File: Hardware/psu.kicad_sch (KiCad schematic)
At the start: 25 parts, among them U3 MP1584EN-LF-P, U4 AMS1117

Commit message: Reannotated
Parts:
- removed D4: D, symbol Device:D
- added D5: SMF3.3A, Diode_SMD:D_SMF, symbol Diode:SMF30A
- renumbered C5 to C10, C6 to C11, C8 to C12, C7 to C5, C9 to C6, C10 to C7, C16 to C8, C4 to C9, D5 to D13, D1 to D3, D3 to D4, D2 to D6, F2 to F1, F1 to F2, R7 to R12, R11 to R13, R8 to R14, R9 to R15, R10 to R16, R15 to R17, R16 to R35, U3 to U5
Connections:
- net +3V3: now also D5.1 (A1)
- net GND: now also D5.2 (A2)

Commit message: Pretty much all components now have values
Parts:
- C10, C9: value C_Polarized -> 100u
- C11, C5, C7, C8: value C -> 100n
- C12: value C -> 150p
- C6: value C_Polarized -> 220u
- D13: value LED -> RED
- D3: value D_Schottky -> SS54
- D4: value D -> B340A-13-F
- F1: value Fuse -> 32V?
- F2: value Fuse -> 1A
- L2: value L -> 15uH/3A
- R12: value R_Small -> 100k
- R13: value R -> 210k
- R14: value R_Small -> 24.9k
- R15, R16: value R -> 100k
- R17: value R -> 40.2k
- R35: value R -> 1k
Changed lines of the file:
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@@
 			)
 		)
-		(property "Value" "Fuse"
+		(property "Value" "32V?"
 			(at 182.88 52.1278 90)
 			(effects
@@
 			)
 		)
-		(property "Value" "R_Small"
+		(property "Value" "100k"
 			(at 113.2586 72.3321 0)
 			(effects
@@
 			)
 		)
-		(property "Value" "R"
+		(property "Value" "1k"
 			(at 231.648 59.6321 0)
 			(effects
@@
 			)
 		)
-		(property "Value" "L"
+		(property "Value" "15uH/3A"
 			(at 162.56 52.07 90)
 			(effects
@@
 			)
 		)
-		(property "Value" "C"
+		(property "Value" "100n"
 			(at 142.24 50.7308 90)
 			(effects
@@
 			)
 		)
-		(property "Value" "Fuse"
+		(property "Value" "1A"
 			(at 59.69 63.5578 90)
 			(effects
@@
 			)
 		)
-		(property "Value" "D_Schottky"
+		(property "Value" "SS54"
 			(at 70.1675 63.0498 0)
 			(effects
@@
 			)
 		)
-		(property "Value" "R_Small"
+		(property "Value" "24.9k"
 			(at 113.2586 83.7621 0)
 			(effects
@@
 			)
 		)
-		(property "Value" "R"
+		(property "Value" "40.2k"
 			(at 177.038 86.3021 0)
 			(effects
@@
 			)
 		)
-		(property "Value" "C"
+		(property "Value" "100n"
 			(at 105.791 77.4121 0)
 			(effects
@@
 			)
 		)
-		(property "Value" "R"
+		(property "Value" "100k"
 			(at 151.638 86.3021 0)
 			(effects
@@
 			)
 		)
-		(property "Value" "LED"
+		(property "Value" "RED"
 			(at 232.791 71.3796 90)
 			(effects
@@
 			)
 		)
-		(property "Value" "R"
+		(property "Value" "210k"
 			(at 177.8 67.31 90)
 			(effects
@@
 			)
 		)
-		(property "Value" "C"
+		(property "Value" "100n"
 			(at 223.901 64.7121 0)
 			(effects
@@
 			)
 		)
-		(property "Value" "C_Polarized"
+		(property "Value" "220u"
 			(at 171.831 61.2831 0)
 			(effects
@@
 			)
 		)
-		(property "Value" "C"
+		(property "Value" "100n"
 			(at 193.421 63.4421 0)
 			(effects
@@
 			)
 		)
-		(property "Value" "C_Polarized"
+		(property "Value" "100u"
 			(at 98.171 76.5231 0)
 			(effects
@@
 			)
 		)
-		(property "Value" "C"
+		(property "Value" "150p"
 			(at 152.781 76.1421 0)
 			(effects
@@
 			)
 		)
-		(property "Value" "D"
+		(property "Value" "B340A-13-F"
 			(at 158.242 62.1721 90)
 			(effects
@@
 			)
 		)
-		(property "Value" "R"
+		(property "Value" "100k"
 			(at 123.698 79.9521 0)
 			(effects
@@
 			)
 		)
-		(property "Value" "C_Polarized"
+		(property "Value" "100u"
 			(at 89.281 76.5231 0)
 			(effects

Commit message: Second cut of circuit board
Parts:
- C11, C12, C5, C7, C8: footprint (none) -> Capacitor_SMD:C_0603_1608Metric
- D13: footprint (none) -> LED_SMD:LED_0603_1608Metric
- D3, D4: footprint (none) -> Diode_SMD:D_SMA
- L2: footprint (none) -> Inductor_SMD:L_SXN_SMDRI64
- R12, R13, R14, R15, R16, R17, R35: footprint (none) -> Resistor_SMD:R_0603_1608Metric
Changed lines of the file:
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@@
 			)
 		)
-		(property "Footprint" ""
+		(property "Footprint" "Resistor_SMD:R_0603_1608Metric"
 			(at 111.76 71.12 0)
 			(effects
@@
 			)
 		)
-		(property "Footprint" ""
+		(property "Footprint" "Resistor_SMD:R_0603_1608Metric"
 			(at 228.092 58.42 90)
 			(effects
@@
 			)
 		)
-		(property "Footprint" ""
+		(property "Footprint" "Inductor_SMD:L_SXN_SMDRI64"
 			(at 162.56 54.61 0)
 			(effects
@@
 			)
 		)
-		(property "Footprint" ""
+		(property "Footprint" "Capacitor_SMD:C_0603_1608Metric"
 			(at 146.05 53.6448 0)
 			(effects
@@
 			)
 		)
-		(property "Footprint" ""
+		(property "Footprint" "Diode_SMD:D_SMA"
 			(at 69.85 66.04 0)
 			(effects
@@
 			)
 		)
-		(property "Footprint" ""
+		(property "Footprint" "Resistor_SMD:R_0603_1608Metric"
 			(at 111.76 82.55 0)
 			(effects
@@
 			)
 		)
-		(property "Footprint" ""
+		(property "Footprint" "Resistor_SMD:R_0603_1608Metric"
 			(at 173.482 85.09 90)
 			(effects
@@
 			)
 		)
-		(property "Footprint" ""
+		(property "Footprint" "Capacitor_SMD:C_0603_1608Metric"
 			(at 101.9048 72.39 0)
 			(effects
@@
 			)
 		)
-		(property "Footprint" ""
+		(property "Footprint" "Resistor_SMD:R_0603_1608Metric"
 			(at 148.082 85.09 90)
 			(effects
@@
 			)
 		)
-		(property "Footprint" ""
+		(property "Footprint" "LED_SMD:LED_0603_1608Metric"
 			(at 229.87 68.58 0)
 			(effects
@@
 			)
 		)
-		(property "Footprint" ""
+		(property "Footprint" "Resistor_SMD:R_0603_1608Metric"
 			(at 173.482 67.31 90)
 			(effects
@@
 			)
 		)
-		(property "Footprint" ""
+		(property "Footprint" "Capacitor_SMD:C_0603_1608Metric"
 			(at 220.0148 59.69 0)
 			(effects
@@
 			)
 		)
-		(property "Footprint" ""
+		(property "Footprint" "Capacitor_SMD:C_0603_1608Metric"
 			(at 189.5348 58.42 0)
 			(effects
@@
 			)
 		)
-		(property "Footprint" ""
+		(property "Footprint" "Capacitor_SMD:C_0603_1608Metric"
 			(at 148.8948 71.12 0)
 			(effects
@@
 			)
 		)
-		(property "Footprint" ""
+		(property "Footprint" "Diode_SMD:D_SMA"
 			(at 156.21 60.96 0)
 			(effects
@@
 			)
 		)
-		(property "Footprint" ""
+		(property "Footprint" "Resistor_SMD:R_0603_1608Metric"
 			(at 120.142 78.74 90)
 			(effects

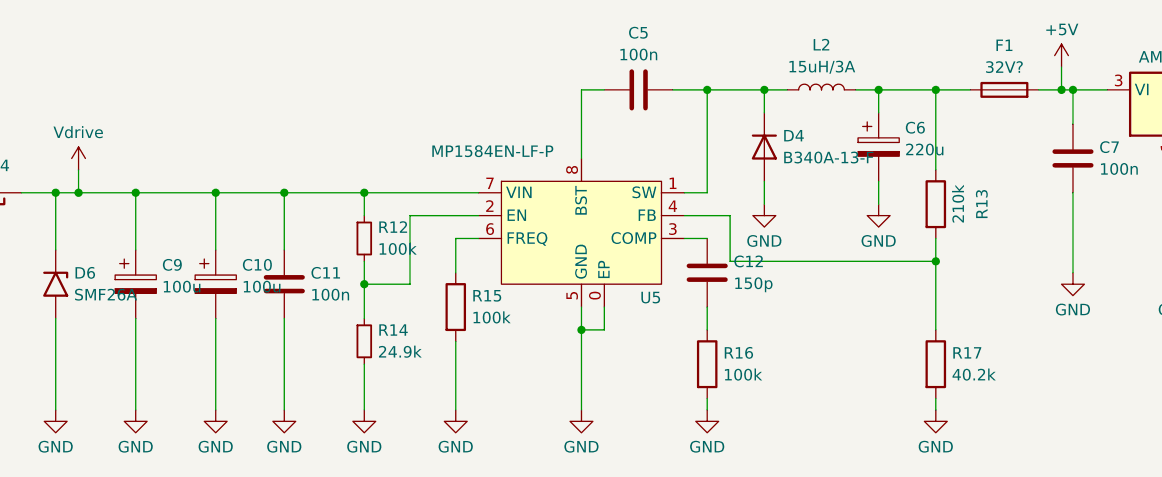
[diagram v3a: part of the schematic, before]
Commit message: Third cut of PCB.  Ready for BoM and routing
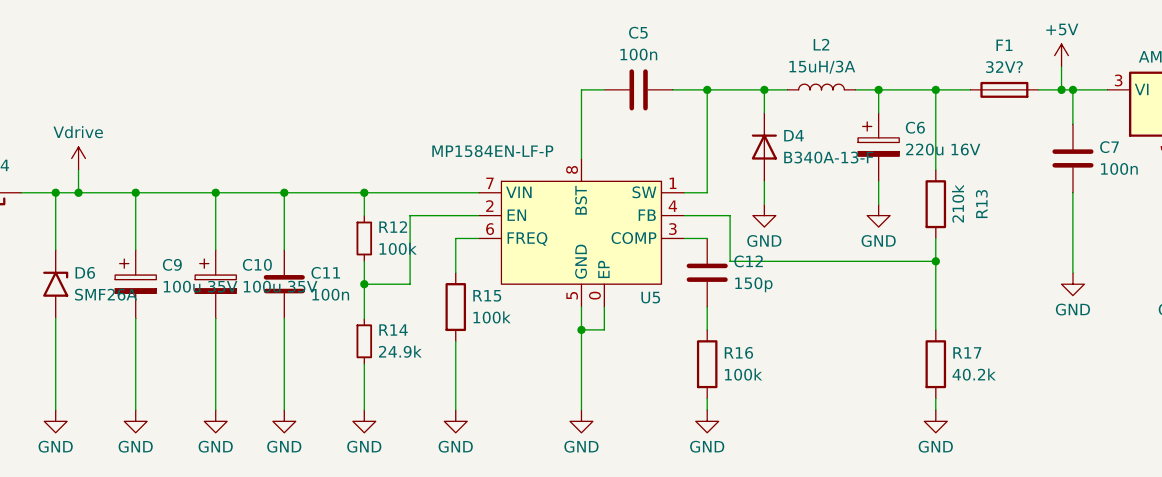
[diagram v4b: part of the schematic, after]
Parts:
- C10, C9: value 100u -> 100u 35V; footprint (none) -> Capacitor_SMD:C_Elec_6.3x5.8
- C6: value 220u -> 220u 16V; footprint (none) -> Capacitor_SMD:C_Elec_6.3x5.8
- D3, D4: footprint Diode_SMD:D_SMA -> Diode_SMD:D_1206_3216Metric
- F1, F2: footprint (none) -> Fuse:Fuse_1206_3216Metric
- U5: footprint :SOIC-8_L4.9-W3.9-P1.27-LS6.0-TL-EP-1 -> esp32-bldc-foc:SOIC-8_L4.9-W3.9-P1.27-LS6.0-TL-EP-1
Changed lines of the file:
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@@
 			)
 		)
-		(property "Footprint" ""
+		(property "Footprint" "Fuse:Fuse_1206_3216Metric"
 			(at 182.88 56.388 90)
 			(effects
@@
 			)
 		)
-		(property "Footprint" ":SOIC-8_L4.9-W3.9-P1.27-LS6.0-TL-EP-1"
+		(property "Footprint" "esp32-bldc-foc:SOIC-8_L4.9-W3.9-P1.27-LS6.0-TL-EP-1"
 			(at 135.89 81.28 0)
 			(effects
@@
 			)
 		)
-		(property "Footprint" ""
+		(property "Footprint" "Fuse:Fuse_1206_3216Metric"
 			(at 59.69 67.818 90)
 			(effects
@@
 			)
 		)
-		(property "Footprint" "Diode_SMD:D_SMA"
+		(property "Footprint" "Diode_SMD:D_1206_3216Metric"
 			(at 69.85 66.04 0)
 			(effects
@@
 			)
 		)
-		(property "Value" "220u"
+		(property "Value" "220u 16V"
 			(at 171.831 61.2831 0)
 			(effects
@@
 			)
 		)
-		(property "Footprint" ""
+		(property "Footprint" "Capacitor_SMD:C_Elec_6.3x5.8"
 			(at 169.8752 64.77 0)
 			(effects
@@
 			)
 		)
-		(property "Value" "100u"
+		(property "Value" "100u 35V"
 			(at 98.171 76.5231 0)
 			(effects
@@
 			)
 		)
-		(property "Footprint" ""
+		(property "Footprint" "Capacitor_SMD:C_Elec_6.3x5.8"
 			(at 96.2152 80.01 0)
 			(effects
@@
 			)
 		)
-		(property "Footprint" "Diode_SMD:D_SMA"
+		(property "Footprint" "Diode_SMD:D_1206_3216Metric"
 			(at 156.21 60.96 0)
 			(effects
@@
 			)
 		)
-		(property "Value" "100u"
+		(property "Value" "100u 35V"
 			(at 89.281 76.5231 0)
 			(effects
@@
 			)
 		)
-		(property "Footprint" ""
+		(property "Footprint" "Capacitor_SMD:C_Elec_6.3x5.8"
 			(at 87.3252 80.01 0)
 			(effects

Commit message: Remove "LCSC Part" field (I use just "LCSC")
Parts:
- U5: LCSC (none) -> C7304223; LCSC Part C7304223 -> (none)
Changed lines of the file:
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@@
 			)
 		)
-		(property "LCSC Part" "C7304223"
-			(at 135.89 83.82 0)
+		(property "LCSC" "C7304223"
+			(at 135.89 69.85 0)
 			(effects
 				(font

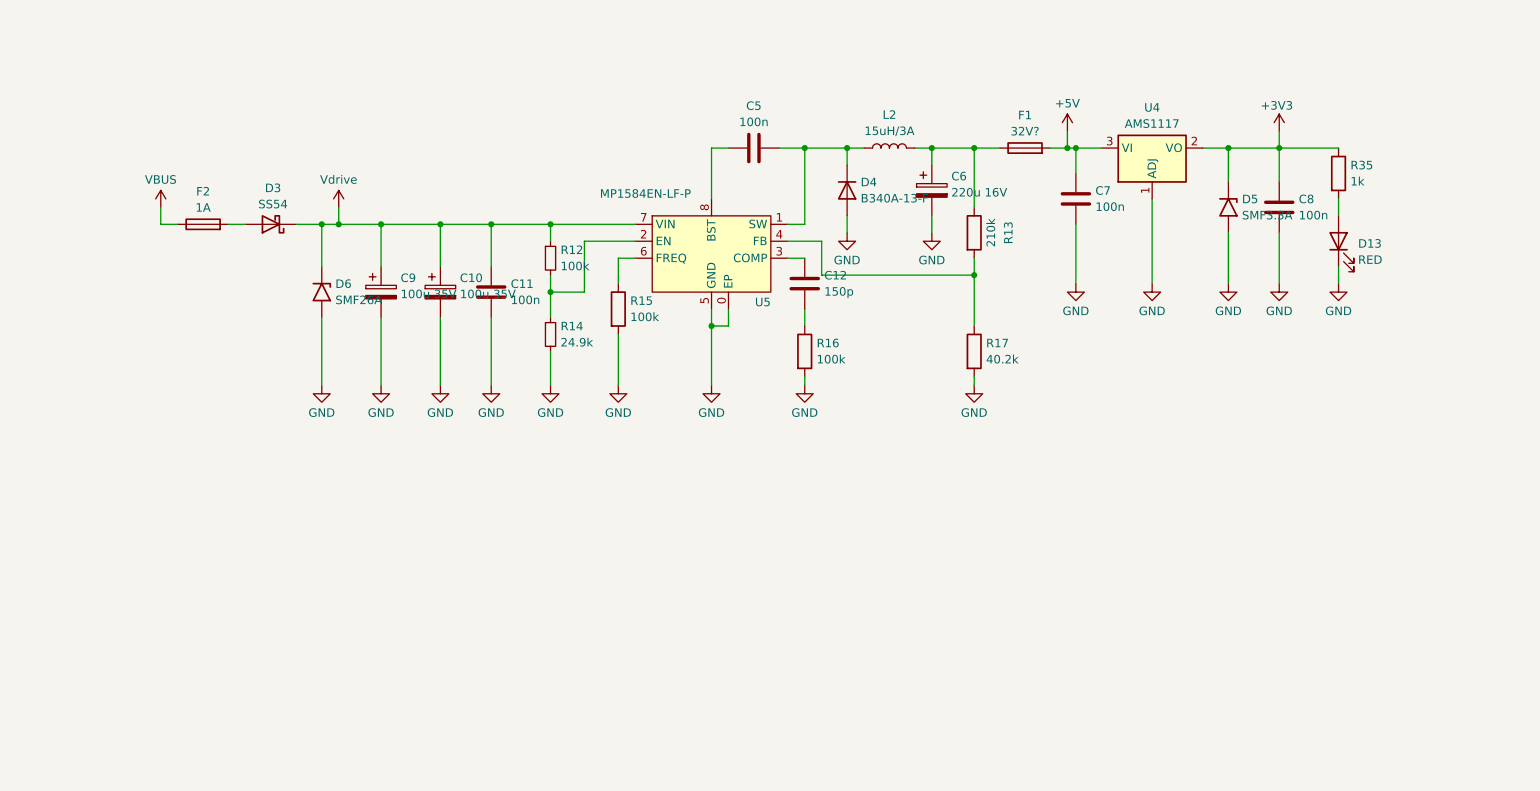
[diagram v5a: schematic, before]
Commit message: Replaced power supply with the one from OpenKayo
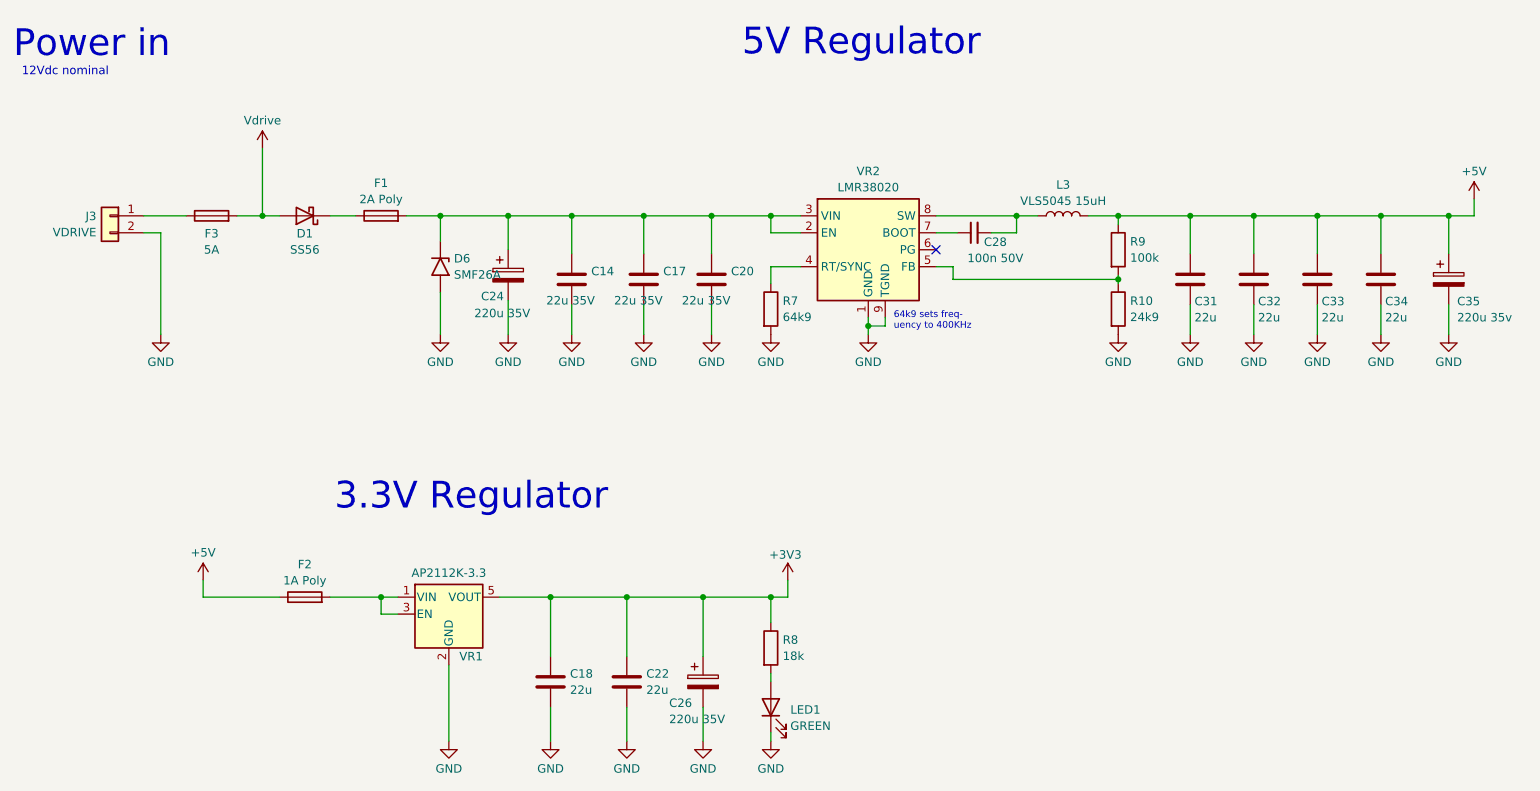
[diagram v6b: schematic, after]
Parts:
- removed C10, C9: 100u 35V, Capacitor_SMD:C_Elec_6.3x5.8, symbol Device:C_Polarized
- removed C11, C5, C7, C8: 100n, Capacitor_SMD:C_0603_1608Metric, symbol Device:C
- removed C12: 150p, Capacitor_SMD:C_0603_1608Metric, symbol Device:C
- removed C6: 220u 16V, Capacitor_SMD:C_Elec_6.3x5.8, symbol Device:C_Polarized
- removed D13: RED, LED_SMD:LED_0603_1608Metric, symbol Device:LED
- removed D3: SS54, Diode_SMD:D_1206_3216Metric, symbol Device:D_Schottky
- removed D4: B340A-13-F, Diode_SMD:D_1206_3216Metric, symbol Device:D
- removed D5: SMF3.3A, Diode_SMD:D_SMF, symbol Diode:SMF30A
- removed L2: 15uH/3A, Inductor_SMD:L_SXN_SMDRI64, symbol Device:L
- removed R12: 100k, Resistor_SMD:R_0603_1608Metric, symbol Device:R_Small
- removed R13: 210k, Resistor_SMD:R_0603_1608Metric, symbol Device:R
- removed R14: 24.9k, Resistor_SMD:R_0603_1608Metric, symbol Device:R_Small
- removed R15, R16: 100k, Resistor_SMD:R_0603_1608Metric, symbol Device:R
- removed R17: 40.2k, Resistor_SMD:R_0603_1608Metric, symbol Device:R
- removed R35: 1k, Resistor_SMD:R_0603_1608Metric, symbol Device:R
- removed U4: AMS1117, Package_TO_SOT_SMD:SOT-223-3_TabPin2, symbol Regulator_Linear:AMS1117
- removed U5: MP1584EN-LF-P, esp32-bldc-foc:SOIC-8_L4.9-W3.9-P1.27-LS6.0-TL-EP-1, symbol esp32-bldc-foc:MP1584EN-LF-P
- added C14, C17, C20: 22u 35V, Capacitor_SMD:C_0805_2012Metric, symbol Device:C
- added C18, C22, C31, C32, C33, C34: 22u, Capacitor_SMD:C_0805_2012Metric, symbol Device:C
- added C24, C26: 220u 35V, Capacitor_SMD:CP_Elec_8x10, symbol Device:C_Polarized
- added C28: 100n 50V, Capacitor_SMD:C_0603_1608Metric, symbol Device:C_Small
- added C35: 220u 35v, Capacitor_SMD:CP_Elec_8x10, symbol Device:C_Polarized
- added D1: SS56, Diode_SMD:D_SMA, symbol Device:D_Schottky
- added F3: 5A, esp32-bldc-foc:Fuseholder_Blade, symbol Device:Fuse
- added J3: VDRIVE, TerminalBlock_MetzConnect:TerminalBlock_MetzConnect_Type086_RT03402HBLC_1x02_P3.81mm_Horizontal, symbol Connector_Generic:Conn_01x02
- added L3: VLS5045 15uH, Inductor_SMD:L_TDK_VLS6045EX_VLS6045AF, symbol Device:L
- added LED1: GREEN, LED_SMD:LED_0603_1608Metric, symbol Device:LED
- added R10: 24k9, Resistor_SMD:R_0603_1608Metric, symbol Device:R
- added R7: 64k9, Resistor_SMD:R_0603_1608Metric, symbol Device:R
- added R8: 18k, Resistor_SMD:R_0603_1608Metric, symbol Device:R
- added R9: 100k, Resistor_SMD:R_0603_1608Metric, symbol Device:R
- added VR1: AP2112K-3.3, Package_TO_SOT_SMD:SOT-23-5, symbol Regulator_Linear:AP2112K-3.3
- added VR2: LMR38020, Package_SO:Texas_HSOP-8-1EP_3.9x4.9mm_P1.27mm_ThermalVias, symbol _:LMR38020
- F1: value 32V? -> 2A Poly; footprint Fuse:Fuse_1206_3216Metric -> esp32-bldc-foc:Fuse_2018_5045Metric
- F2: value 1A -> 1A Poly
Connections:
- net VBUS is gone; now on net +5V: F2.1
- net +3V3: now also C18.1, C22.1, C26.1, R8.1, VR1.5 (VOUT)
- net +5V: now also C31.1, C32.1, C33.1, C34.1, C35.1, L3.2, R9.1; no longer F1.2
- net GND: now also C14.2, C17.2, C18.2, C20.2, C22.2, C24.2, C26.2, C31.2, C32.2, C33.2, C34.2, C35.2, J3.2 (Pin_2), LED1.1 (K), R10.2, R7.2, VR1.2 (GND), VR2.1 (GND), VR2.9 (TGND)
- net Vdrive: now also D1.2 (A), F3.2; no longer D6.1 (A1)
- net at F1.1: now also D1.1 (K)
- net at F2.2: now also VR1.1 (VIN), VR1.3 (EN)
- new net: C14.1, C17.1, C20.1, C24.1, D6.1 (A1), F1.2, VR2.2 (EN), VR2.3 (VIN)
- new net: F3.1, J3.1 (Pin_1)
- new net: LED1.2 (A), R8.2
- new net: R7.1, VR2.4 (RT/SYNC)
- new net: C28.1, VR2.7 (BOOT)
- new net: C28.2, L3.1, VR2.8 (SW)
- new net: R10.1, R9.2, VR2.5 (FB)
- no-connect marks 0 -> 1
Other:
- note added: "12Vdc nominal"
- note added: "3.3V Regulator"
- note added: "5V Regulator"
- note added: "64k9 sets freq- uency to 400KHz"
- note added: "Power in"
- moved on the sheet: D6, F2
